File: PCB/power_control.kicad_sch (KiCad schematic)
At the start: 15 parts

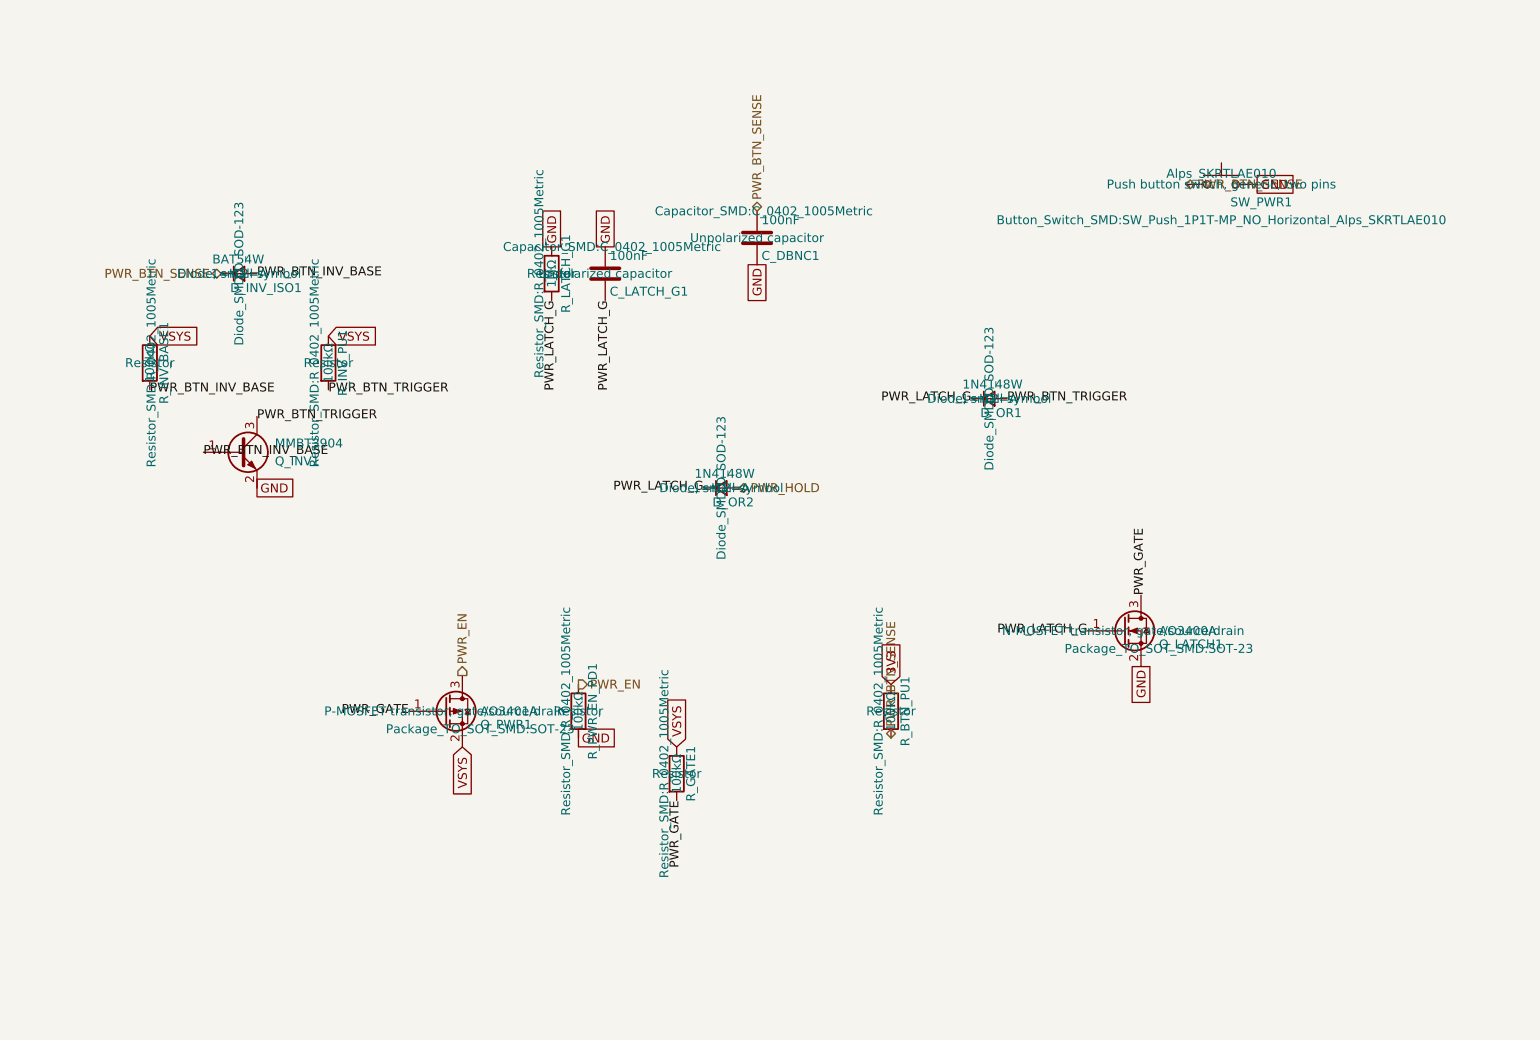
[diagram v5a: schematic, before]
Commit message: fix: make every BOM Value unambiguous for the fab, and switch D_INV_ISO1 to SOT-323 (#61)
* fix: make every BOM Value unambiguous for the fab, and switch D_INV_ISO1 to SOT-323

PCBWay flagged D_INV_ISO1: "BAT54W" is SOT-323 from nearly every maker, but we
had picked Yangjie's SOD-123 variant. A fab only sees Designator, Footprint,
Quantity and Value in the BOM (never MF/MPN/LCSC), so a bare part name is
ambiguous. Fixes the class of problem, not just this part:

- Every component's Value is now "<label> | <MPN> | <manufacturer> | <package>"
  (label dropped when it repeats the MPN; commas/periods stripped so the CSV
  never needs quoting). BT1 keeps its RIGHT-ANGLE HORIZONTAL note. Applied to
  all 81 parts across every sheet and the PCB.
- scripts/bom_values.py builds, applies, and checks these values, including
  that the PCB copy of Value/MF/MPN/footprint matches the schematic. New
  footprints must be added to its package table on purpose; hand-sourced parts
  with no MPN (J_STICK1) are listed explicitly.
- D_INV_ISO1 -> Diodes BAT54W-7-F in SOT-323 (common part, several makers).
  Pin 1 anode / pin 2 not connected / pin 3 cathode, confirmed against
  Nexperia's numbered pinning table and Diodes' datasheet. Uses KiCad's
  Diode:BAT54W symbol; PCB footprint replaced and rerouted. Electrically the
  same BAT54 family (30V, 200mA, 2uA leakage at 25V), so the SPICE model and
  scripts/spice/latch_sim.py still pass.
- Layout diagrams now say AO3401A for Q_PWR1 (they were stale since it was
  swapped from DMG2305UX) and BAT54W-7-F/SOT-323 for D_INV_ISO1.
- Repo CLAUDE.md documents the Value rule and the script.

ERC/DRC clean; production files regenerated.

Co-Authored-By: Claude Sonnet 5 <noreply@anthropic.com>

* chore: commit KiCad project settings (reordered used-designators list)

Co-Authored-By: Claude Sonnet 5 <noreply@anthropic.com>

---------

Co-authored-by: Claude Sonnet 5 <noreply@anthropic.com>
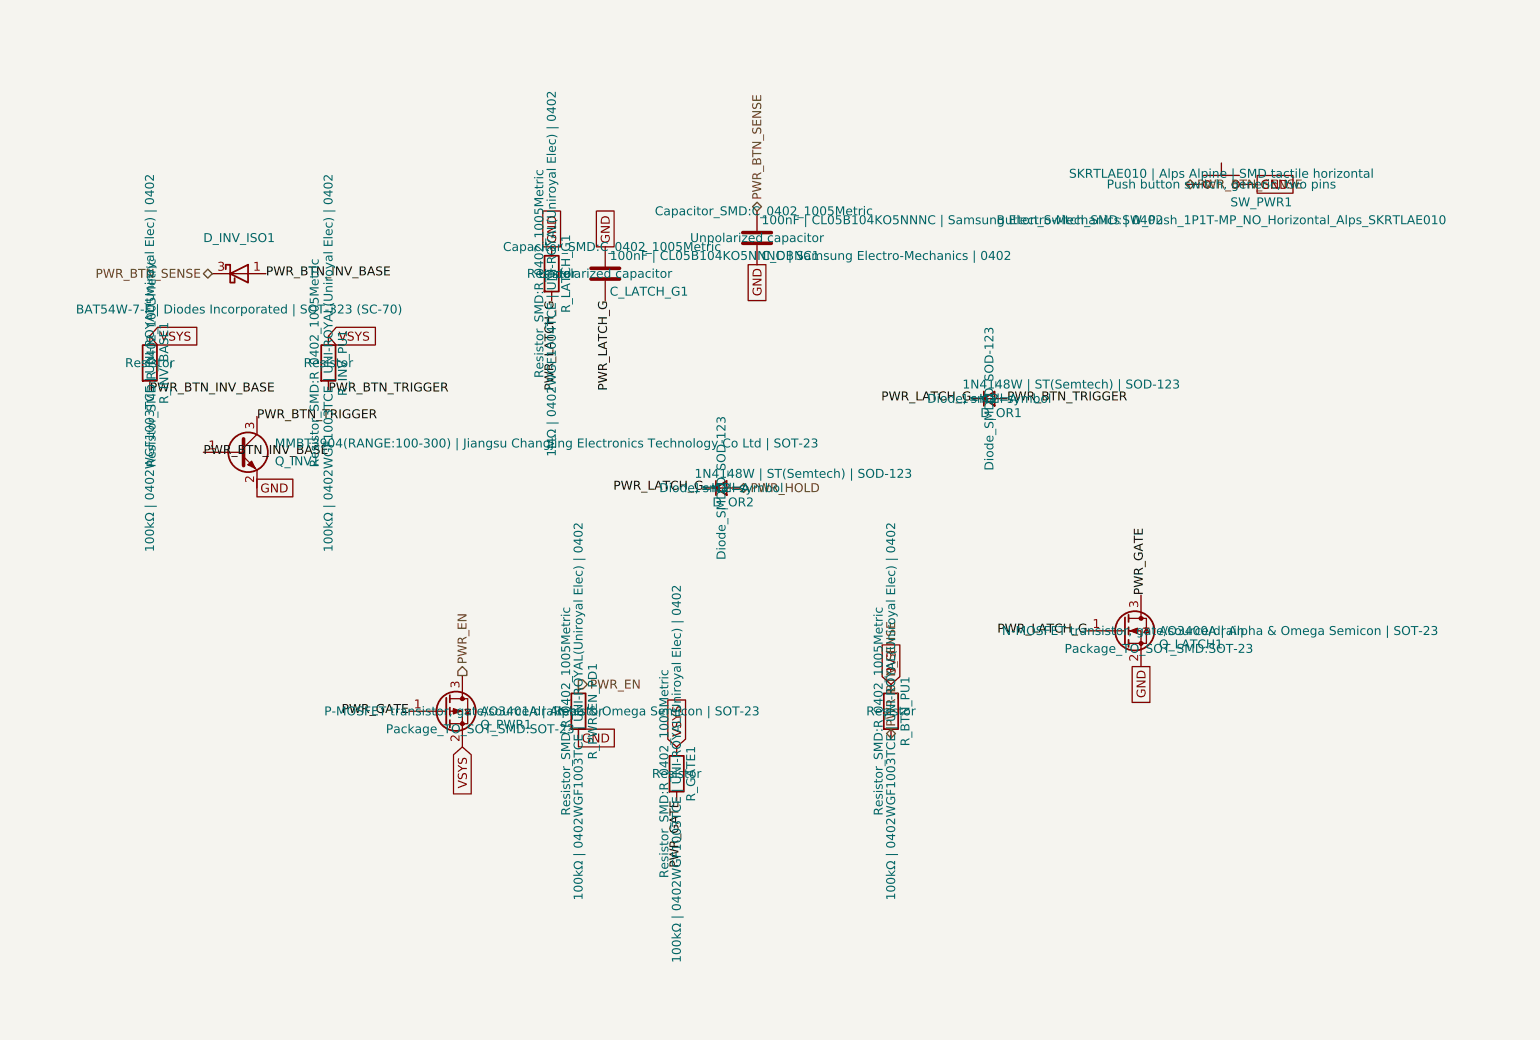
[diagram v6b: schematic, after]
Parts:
- C_DBNC1, C_LATCH_G1: value 100nF -> 100nF | CL05B104KO5NNNC | Samsung Electro-Mechanics | 0402
- D_INV_ISO1: value BAT54W -> BAT54W-7-F | Diodes Incorporated | SOT-323 (SC-70); footprint Diode_SMD:D_SOD-123 -> Package_TO_SOT_SMD:SOT-323_SC-70; symbol Device:D_Small -> Diode:BAT54W; LCSC C699107 -> C134417; MF Yangzhou Yangjie Elec Tech -> Diodes Incorporated; Manufacturer_Part_Number BAT54W -> BAT54W-7-F
- D_OR1, D_OR2: value 1N4148W -> 1N4148W | ST(Semtech) | SOD-123
- Q_INV1: value MMBT3904 -> MMBT3904(RANGE:100-300) | Jiangsu Changjing Electronics Technology Co Ltd | SOT-23
- Q_LATCH1: value AO3400A -> AO3400A | Alpha & Omega Semicon | SOT-23
- Q_PWR1: value AO3401A -> AO3401A | Alpha & Omega Semicon | SOT-23
- R_BTN_PU1, R_GATE1, R_INV_BASE1, R_INV_PU1, R_PWR_EN_PD1: value 100kΩ -> 100kΩ | 0402WGF1003TCE | UNI-ROYAL(Uniroyal Elec) | 0402
- R_LATCH_G1: value 1MΩ -> 1MΩ | 0402WGF1004TCE | UNI-ROYAL(Uniroyal Elec) | 0402
- SW_PWR1: value Alps_SKRTLAE010 -> SKRTLAE010 | Alps Alpine | SMD tactile horizontal
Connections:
- net PWR_BTN_INV_BASE: now also D_INV_ISO1.1 (A); no longer D_INV_ISO1.2 (A)
- net PWR_BTN_SENSE: now also D_INV_ISO1.3 (K); no longer D_INV_ISO1.1 (K)
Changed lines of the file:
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@@
 	)
 	(label "PWR_BTN_INV_BASE"
-		(at 66.04 76.2 0)
+		(at 67.31 76.2 0)
 		(effects
 			(font
@@
 	(hierarchical_label "PWR_BTN_SENSE"
 		(shape bidirectional)
-		(at 60.96 76.2 180)
+		(at 59.69 76.2 180)
 		(effects
 			(font
@@
 			)
 		)
-		(property "Value" "100kΩ"
+		(property "Value" "100kΩ | 0402WGF1003TCE | UNI-ROYAL(Uniroyal Elec) | 0402"
 			(at 76.2 88.9 90)
 			(show_name no)
@@
 			)
 		)
-		(property "Value" "100kΩ"
+		(property "Value" "100kΩ | 0402WGF1003TCE | UNI-ROYAL(Uniroyal Elec) | 0402"
 			(at 50.8 88.9 90)
 			(show_name no)
@@
 			)
 		)
-		(property "Value" "100nF"
+		(property "Value" "100nF | CL05B104KO5NNNC | Samsung Electro-Mechanics | 0402"
 			(at 137.795 68.58 0)
 			(show_name no)
@@
 			)
 		)
-		(property "Value" "Alps_SKRTLAE010"
+		(property "Value" "SKRTLAE010 | Alps Alpine | SMD tactile horizontal"
 			(at 203.2 61.976 0)
 			(show_name no)
@@
 			)
 		)
-		(property "Value" "AO3401A"
+		(property "Value" "AO3401A | Alpha & Omega Semicon | SOT-23"
 			(at 97.79 138.43 0)
 			(show_name no)
@@
 			)
 		)
-		(property "Value" "1N4148W"
+		(property "Value" "1N4148W | ST(Semtech) | SOD-123"
 			(at 128.27 104.648 0)
 			(show_name no)
@@
 			)
 		)
-		(property "Value" "100kΩ"
+		(property "Value" "100kΩ | 0402WGF1003TCE | UNI-ROYAL(Uniroyal Elec) | 0402"
 			(at 156.21 138.43 90)
 			(show_name no)
@@
 			)
 		)
-		(property "Value" "1MΩ"
+		(property "Value" "1MΩ | 0402WGF1004TCE | UNI-ROYAL(Uniroyal Elec) | 0402"
 			(at 107.95 76.2 90)
 			(show_name no)
@@
 			)
 		)
-		(property "Value" "100kΩ"
+		(property "Value" "100kΩ | 0402WGF1003TCE | UNI-ROYAL(Uniroyal Elec) | 0402"
 			(at 125.73 147.32 90)
 			(show_name no)
@@
 			)
 		)
-		(property "Value" "1N4148W"
+		(property "Value" "1N4148W | ST(Semtech) | SOD-123"
 			(at 166.37 91.948 0)
 			(show_name no)
@@
 			)
 		)
-		(property "Value" "100kΩ"
+		(property "Value" "100kΩ | 0402WGF1003TCE | UNI-ROYAL(Uniroyal Elec) | 0402"
 			(at 111.76 138.43 90)
 			(show_name no)
@@
 			)
 		)
-		(property "Value" "100nF"
+		(property "Value" "100nF | CL05B104KO5NNNC | Samsung Electro-Mechanics | 0402"
 			(at 116.205 73.66 0)
 			(show_name no)
@@
 	)
 	(symbol
-		(lib_id "Device:D_Small")
+		(lib_id "Diode:BAT54W")
 		(at 63.5 76.2 0)
 		(unit 1)
@@
 		(fields_autoplaced yes)
 		(property "Reference" "D_INV_ISO1"
-			(at 62.23 78.232 0)
-			(show_name no)
-			(do_not_autoplace no)
-			(effects
-				(font
-					(size 1.27 1.27)
-				)
-				(justify left)
-			)
-		)
-		(property "Value" "BAT54W"
-			(at 59.69 74.168 0)
-			(show_name no)
-			(do_not_autoplace no)
-			(effects
-				(font
-					(size 1.27 1.27)
-				)
-				(justify left)
-			)
-		)
-		(property "Footprint" "Diode_SMD:D_SOD-123"
-			(at 63.5 76.2 90)
-			(show_name no)
-			(do_not_autoplace no)
-			(effects
-				(font
-					(size 1.27 1.27)
-				)
-			)
-		)
-		(property "Datasheet" ""
-			(at 63.5 76.2 90)
-			(show_name no)
-			(do_not_autoplace no)
-			(effects
-				(font
-					(size 1.27 1.27)
-				)
-			)
-		)
-		(property "Description" "Diode, small symbol"
+			(at 63.5 71.12 0)
+			(show_name no)
+			(do_not_autoplace no)
+			(effects
+				(font
+					(size 1.27 1.27)
+				)
+			)
+		)
+		(property "Value" "BAT54W-7-F | Diodes Incorporated | SOT-323 (SC-70)"
+			(at 63.5 81.28 0)
+			(show_name no)
+			(do_not_autoplace no)
+			(effects
+				(font
+					(size 1.27 1.27)
+				)
+			)
+		)
+		(property "Footprint" "Package_TO_SOT_SMD:SOT-323_SC-70"
 			(at 63.5 76.2 0)
-			(show_name no)
-			(do_not_autoplace no)
-			(effects
-				(font
-					(size 1.27 1.27)
-				)
-			)
-		)
-		(property "Sim.Device" "D"
+			(hide yes)
+			(show_name no)
+			(do_not_autoplace no)
+			(effects
+				(font
+					(size 1.27 1.27)
+				)
+			)
+		)
+		(property "Datasheet" "https://www.diodes.com/assets/Datasheets/ds30065.pdf"
 			(at 63.5 76.2 0)
-			(show_name no)
-			(do_not_autoplace no)
-			(effects
-				(font
-					(size 1.27 1.27)
-				)
-			)
-		)
-		(property "Sim.Pins" "1=K 2=A"
+			(hide yes)
+			(show_name no)
+			(do_not_autoplace no)
+			(effects
+				(font
+					(size 1.27 1.27)
+				)
+			)
+		)
+		(property "Description" "Schottky barrier diode, SOT-323. Pin 1 anode, pin 2 no-connect, pin 3 cathode."
 			(at 63.5 76.2 0)
-			(show_name no)
-			(do_not_autoplace no)
-			(effects
-				(font
-					(size 1.27 1.27)
-				)
-			)
-		)
-		(property "MF" "Yangzhou Yangjie Elec Tech"
-			(at 0 0 0)
-			(hide yes)
-			(show_name no)
-			(do_not_autoplace no)
-			(effects
-				(font
-					(size 1.27 1.27)
-				)
-			)
-		)
-		(property "Manufacturer_Part_Number" "BAT54W"
-			(at 0 0 0)
-			(hide yes)
-			(show_name no)
-			(do_not_autoplace no)
-			(effects
-				(font
-					(size 1.27 1.27)
-				)
-			)
-		)
-		(property "LCSC" "C699107"
+			(hide yes)
+			(show_name no)
+			(do_not_autoplace no)
+			(effects
+				(font
+					(size 1.27 1.27)
+				)
+			)
+		)
+		(property "MF" "Diodes Incorporated"
+			(at 0 0 0)
+			(hide yes)
+			(show_name no)
+			(do_not_autoplace no)
+			(effects
+				(font
+					(size 1.27 1.27)
+				)
+			)
+		)
+		(property "Manufacturer_Part_Number" "BAT54W-7-F"
+			(at 0 0 0)
+			(hide yes)
+			(show_name no)
+			(do_not_autoplace no)
+			(effects
+				(font
+					(size 1.27 1.27)
+				)
+			)
+		)
+		(property "LCSC" "C134417"
 			(at 0 0 0)
 			(hide yes)
@@
 		)
 		(pin "2"
+		)
+		(pin "3"
 		)
 		(instances
@@
 			)
 		)
-		(property "Value" "MMBT3904"
+		(property "Value" "MMBT3904(RANGE:100-300) | Jiangsu Changjing Electronics Technology Co Ltd | SOT-23"
 			(at 68.58 100.33 0)
 			(show_name no)
@@
 			)
 		)
-		(property "Value" "AO3400A"
+		(property "Value" "AO3400A | Alpha & Omega Semicon | SOT-23"
 			(at 194.31 127 0)
 			(show_name no)
